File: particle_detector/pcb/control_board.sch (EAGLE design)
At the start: 29 parts, among them IC1 LT1807R, IC3 LT3461, IC4 TEENSY 3.2

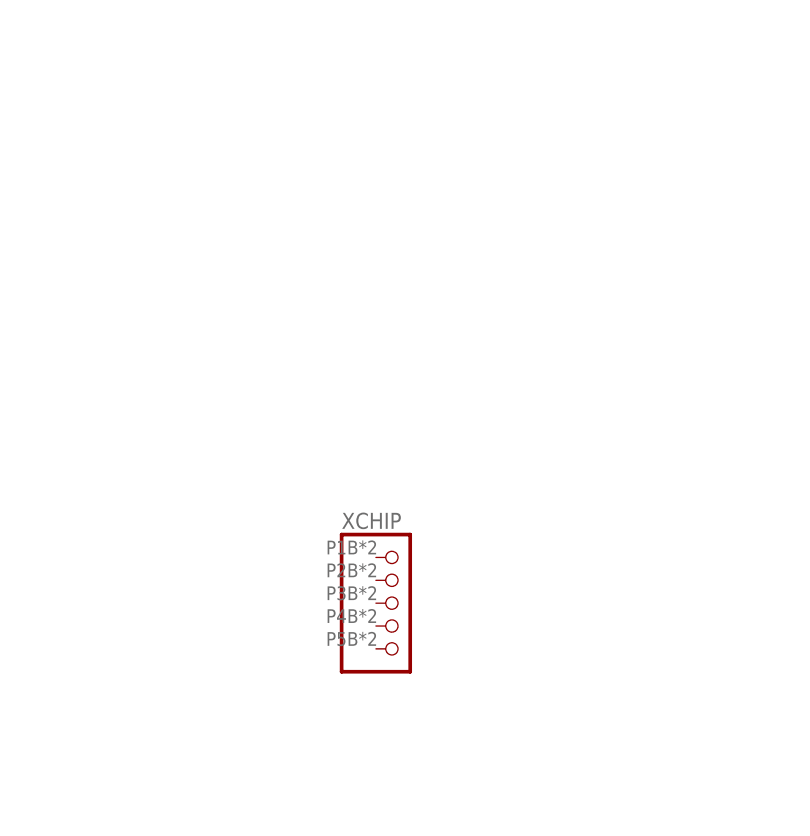
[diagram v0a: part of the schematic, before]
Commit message: update EDA with xinabox footprint; board done, awaiting fabhouse confirmation
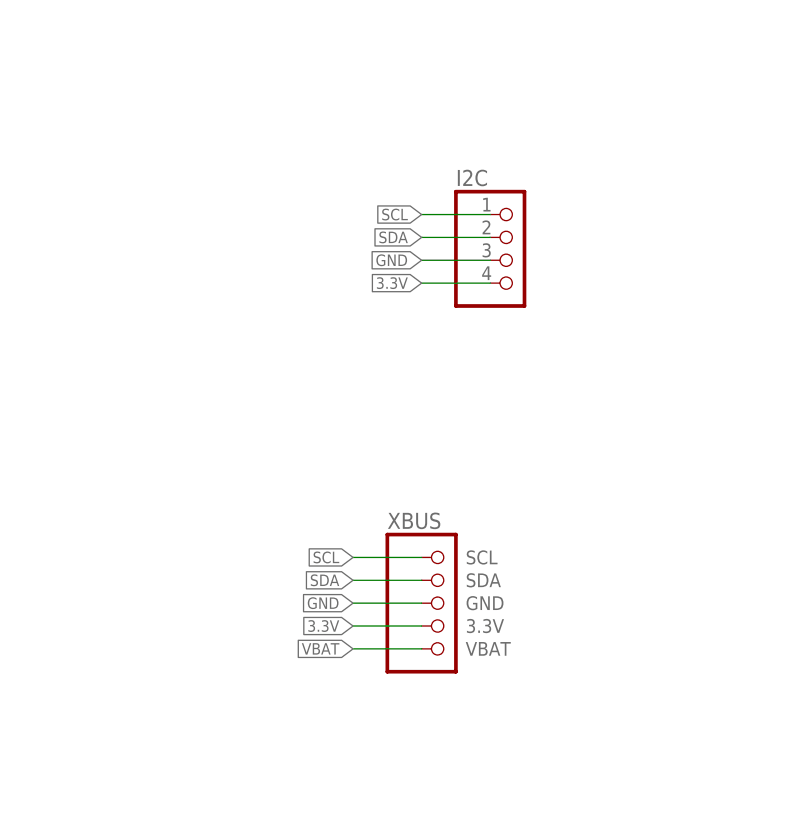
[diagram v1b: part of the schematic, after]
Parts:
- removed XCHIP: (no value), personal:XCHIP-1X5
- added I2C: (no value), pinhead:PINHD-1X4
- added XBUS: (no value), personal:XINABOX-XBUS
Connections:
- new net 3.3V: I2C.4, XBUS.3.3V
- new net VBAT: XBUS.VBAT
- net GND: now also I2C.3, XBUS.GND
- net SCL: now also I2C.1, XBUS.SCL
- net SDA: now also I2C.2, XBUS.SDA
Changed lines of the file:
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@@
 <part name="GND22" library="supply1" library_urn="urn:adsk.eagle:library:371" deviceset="GND" device=""/>
 <part name="GND23" library="supply1" library_urn="urn:adsk.eagle:library:371" deviceset="GND" device=""/>
-<part name="XCHIP" library="personal" deviceset="XCHIP-1X5" device=""/>
 <part name="SIPM" library="pinhead" library_urn="urn:adsk.eagle:library:325" deviceset="PINHD-2X3" device="" package3d_urn="urn:adsk.eagle:package:22462/2"/>
 <part name="GND1" library="supply1" library_urn="urn:adsk.eagle:library:371" deviceset="GND" device=""/>
 <part name="GND2" library="supply1" library_urn="urn:adsk.eagle:library:371" deviceset="GND" device=""/>
+<part name="XBUS" library="personal" deviceset="XINABOX-XBUS" device=""/>
+<part name="I2C" library="pinhead" library_urn="urn:adsk.eagle:library:325" deviceset="PINHD-1X4" device="" package3d_urn="urn:adsk.eagle:package:22407/2"/>
 </parts>
 <sheets>
@@
 <instance part="GND22" gate="1" x="254" y="170.18"/>
 <instance part="GND23" gate="1" x="317.5" y="210.82"/>
-<instance part="XCHIP" gate="G$1" x="365.76" y="127"/>
 <instance part="SIPM" gate="A" x="137.16" y="185.42" rot="R180"/>
 <instance part="GND1" gate="1" x="149.86" y="180.34"/>
 <instance part="GND2" gate="1" x="121.92" y="180.34"/>
+<instance part="XBUS" gate="G$1" x="370.84" y="127"/>
+<instance part="I2C" gate="A" x="378.46" y="165.1"/>
 </instances>
 <busses>
@@
 <pinref part="GND1" gate="1" pin="GND"/>
 <wire x1="149.86" y1="185.42" x2="149.86" y2="182.88" width="0.1524" layer="91"/>
+</segment>
+<segment>
+<pinref part="XBUS" gate="G$1" pin="GND"/>
+<wire x1="368.3" y1="127" x2="360.68" y2="127" width="0.1524" layer="91"/>
+<label x="360.68" y="127" size="1.27" layer="95" rot="R180" xref="yes"/>
+</segment>
+<segment>
+<pinref part="I2C" gate="A" pin="3"/>
+<wire x1="375.92" y1="165.1" x2="368.3" y2="165.1" width="0.1524" layer="91"/>
+<label x="368.3" y="165.1" size="1.27" layer="95" rot="R180" xref="yes"/>
 </segment>
 </net>
@@
 <label x="266.7" y="177.8" size="1.27" layer="95" rot="R180" xref="yes"/>
 </segment>
+<segment>
+<pinref part="XBUS" gate="G$1" pin="SDA"/>
+<wire x1="368.3" y1="129.54" x2="360.68" y2="129.54" width="0.1524" layer="91"/>
+<label x="360.68" y="129.54" size="1.27" layer="95" rot="R180" xref="yes"/>
+</segment>
+<segment>
+<pinref part="I2C" gate="A" pin="2"/>
+<wire x1="375.92" y1="167.64" x2="368.3" y2="167.64" width="0.1524" layer="91"/>
+<label x="368.3" y="167.64" size="1.27" layer="95" rot="R180" xref="yes"/>
+</segment>
 </net>
 <net name="SCL" class="0">
@@
 <label x="266.7" y="175.26" size="1.27" layer="95" rot="R180" xref="yes"/>
 </segment>
-</net>
+<segment>
+<pinref part="XBUS" gate="G$1" pin="SCL"/>
+<wire x1="368.3" y1="132.08" x2="360.68" y2="132.08" width="0.1524" layer="91"/>
+<label x="360.68" y="132.08" size="1.27" layer="95" rot="R180" xref="yes"/>
+</segment>
+<segment>
+<pinref part="I2C" gate="A" pin="1"/>
+<wire x1="375.92" y1="170.18" x2="368.3" y2="170.18" width="0.1524" layer="91"/>
+<label x="368.3" y="170.18" size="1.27" layer="95" rot="R180" xref="yes"/>
+</segment>
+</net>
+<net name="3.3V" class="0">
+<segment>
+<pinref part="XBUS" gate="G$1" pin="3.3V"/>
+<wire x1="368.3" y1="124.46" x2="360.68" y2="124.46" width="0.1524" layer="91"/>
+<label x="360.68" y="124.46" size="1.27" layer="95" rot="R180" xref="yes"/>
+</segment>
+<segment>
+<pinref part="I2C" gate="A" pin="4"/>
+<wire x1="375.92" y1="162.56" x2="368.3" y2="162.56" width="0.1524" layer="91"/>
+<label x="368.3" y="162.56" size="1.27" layer="95" rot="R180" xref="yes"/>
+</segment>
+</net>
+<net name="VBAT" class="0">
+<segment>
+<pinref part="XBUS" gate="G$1" pin="VBAT"/>
+<wire x1="368.3" y1="121.92" x2="360.68" y2="121.92" width="0.1524" layer="91"/>
+<label x="360.68" y="121.92" size="1.27" layer="95" rot="R180" xref="yes"/>
+</segment>
+</net>

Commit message: fix AGNd and 3.3V issue; needs DRC
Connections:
- new net AGND: C6.2, C7.2, C8.2, IC1P.V-, IC4.AGND, R4.1, R6.1, R7.1, R9.1
- net 3.3V: now also IC4.3.3V
- net GND: no longer C6.2, C7.2, C8.2, IC1P.V-, R4.1, R6.1, R7.1, R9.1
